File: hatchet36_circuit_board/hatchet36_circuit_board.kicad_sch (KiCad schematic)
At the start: 82 parts, among them J1 Conn_01x04_Female, SW1 SW_Push, SW10 SW_Push, SW11 SW_Push, SW12 SW_Push, SW13 SW_Push, SW14 SW_Push, SW15 SW_Push, SW16 SW_Push, SW17 SW_Push, SW18 SW_Push, SW19 SW_Push, SW2 SW_Push, SW20 SW_Push, SW21 SW_Push, SW22 SW_Push, SW23 SW_Push, SW24 SW_Push, SW25 SW_Push, SW26 SW_Push, SW27 SW_Push, SW28 SW_Push, SW29 SW_Push, SW3 SW_Push, SW30 SW_Push, SW31 SW_Push, SW32 SW_Push, SW33 SW_Push, SW34 SW_Push, SW35 SW_Push, SW36 SW_Push, SW37 SW_Push, SW38 SW_SPDT, SW4 SW_Push, SW5 SW_Push, SW6 SW_Push, SW7 SW_Push, SW8 SW_Push, SW9 SW_Push, U1 BL652

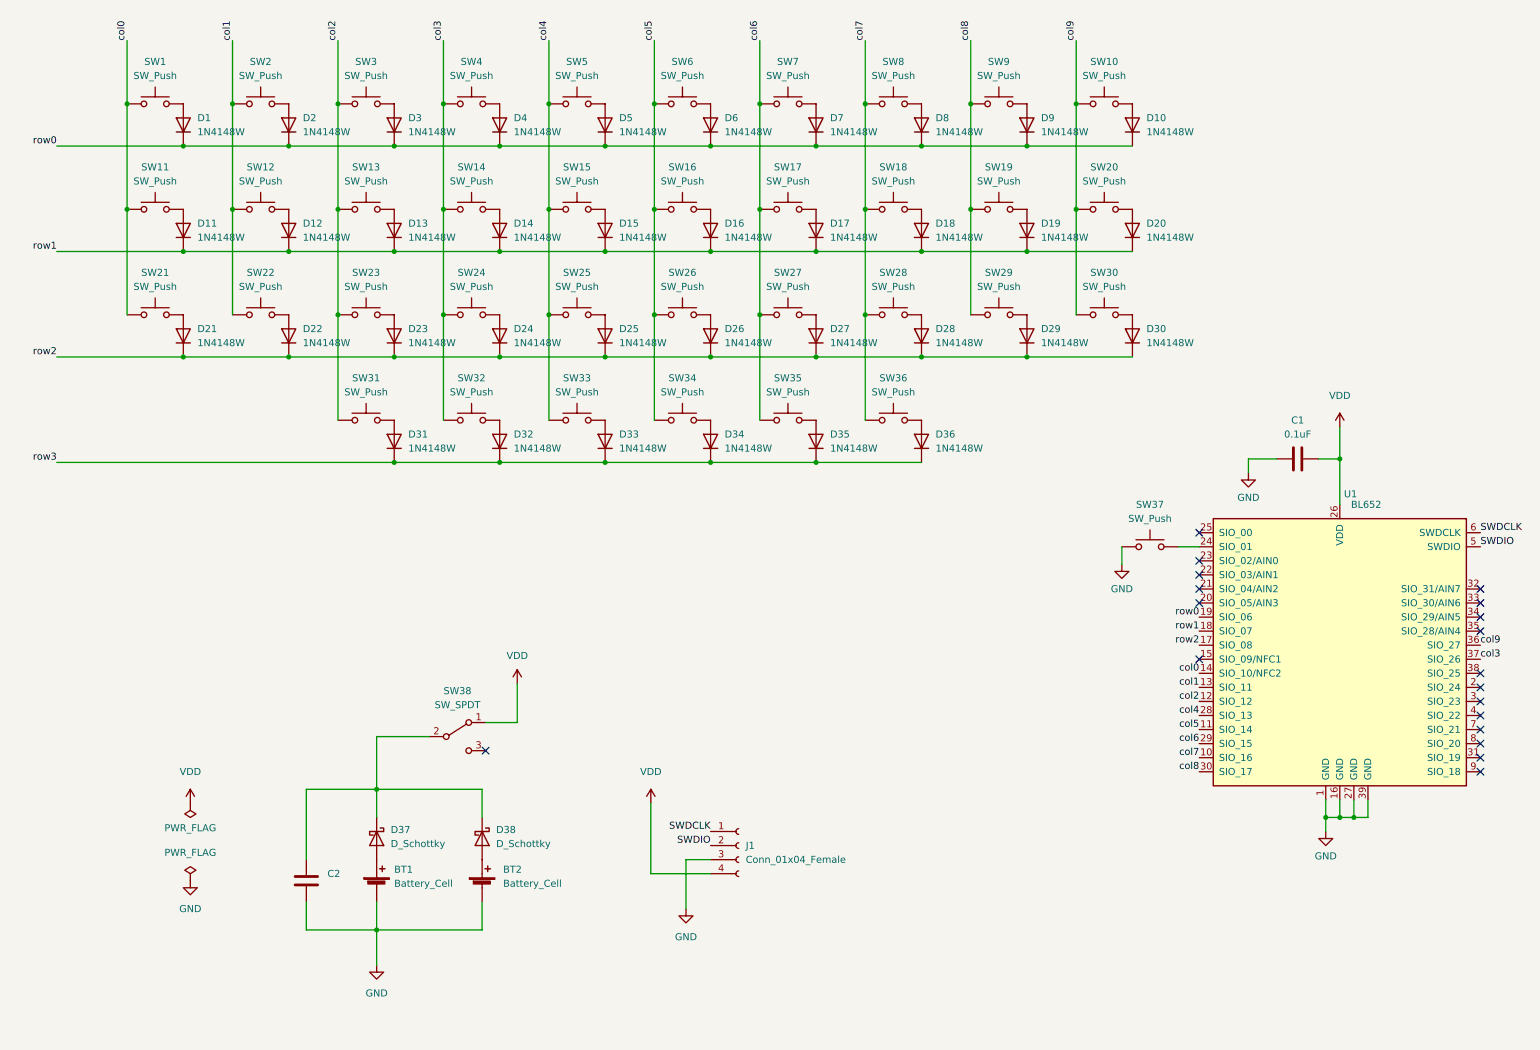
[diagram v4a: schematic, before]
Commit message: add connector
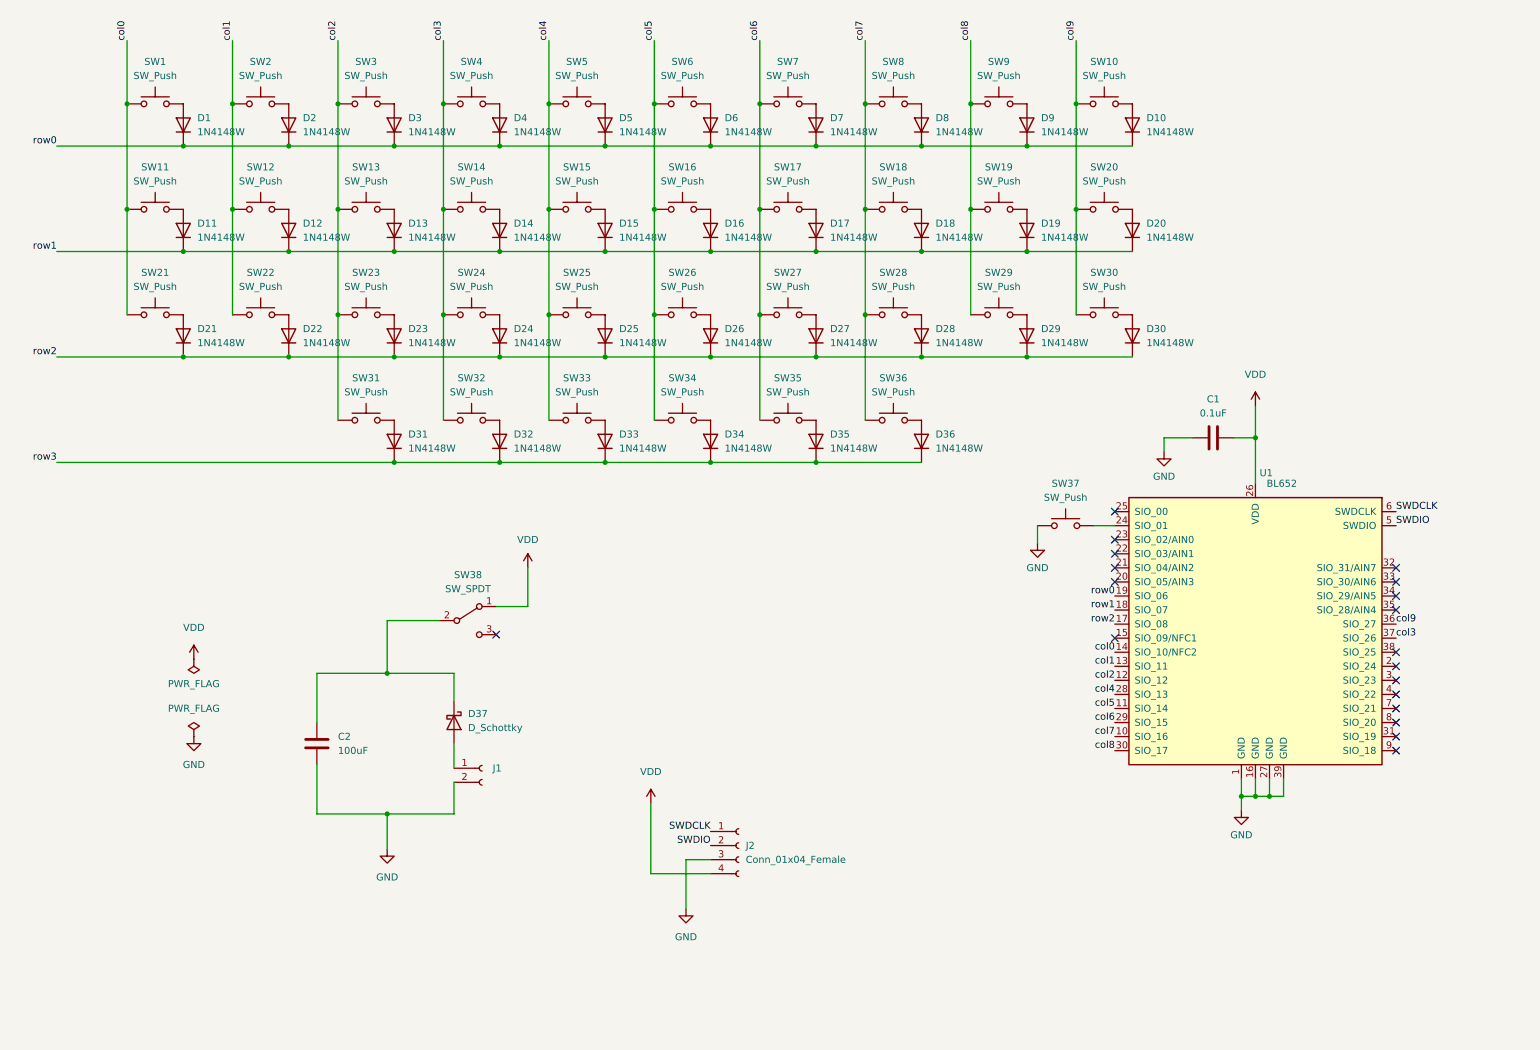
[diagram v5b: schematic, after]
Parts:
- removed BT1, BT2: Battery_Cell, symbol Device:Battery_Cell
- removed D37: D_Schottky, symbol Device:D_Schottky
- added J1: (no value), symbol Connector:Conn_01x02_Female
- C1: footprint (none) -> Capacitor_SMD:C_0805_2012Metric_Pad1.18x1.45mm_HandSolder
- C2: value (none) -> 100uF; footprint (none) -> Capacitor_SMD:C_1206_3216Metric_Pad1.33x1.80mm_HandSolder
- D37: renamed from D38; footprint (none) -> Diode_SMD:D_SOD-323
- J2: renamed from J1; footprint (none) -> locallib:programming_port
- SW1, SW10, SW11, SW12, SW13, SW14, SW15, SW16, SW17, SW18, SW19, SW2, SW20, SW21, SW22, SW23, SW24, SW25, SW26, SW27, SW28, SW29, SW3, SW30, SW31, SW32, SW33, SW34, SW35, SW36, SW4, SW5, SW6, SW7, SW8, SW9: footprint (none) -> locallib:Kailh-PG1350-1u-NoLED-mod
- SW37: footprint (none) -> locallib:SW_SPST_ALPS-SKRP
- SW38: footprint (none) -> locallib:slide_switch_vertical_01x03_pitch2mm
- U1: footprint (none) -> locallib:Laird_BL652_LongPad
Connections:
- net GND: now also J1.2 (Pin_2)
- net at D37.2 (A): now also J1.1 (Pin_1)
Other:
- moved on the sheet: C1, C2, D37, SW37, SW38, U1

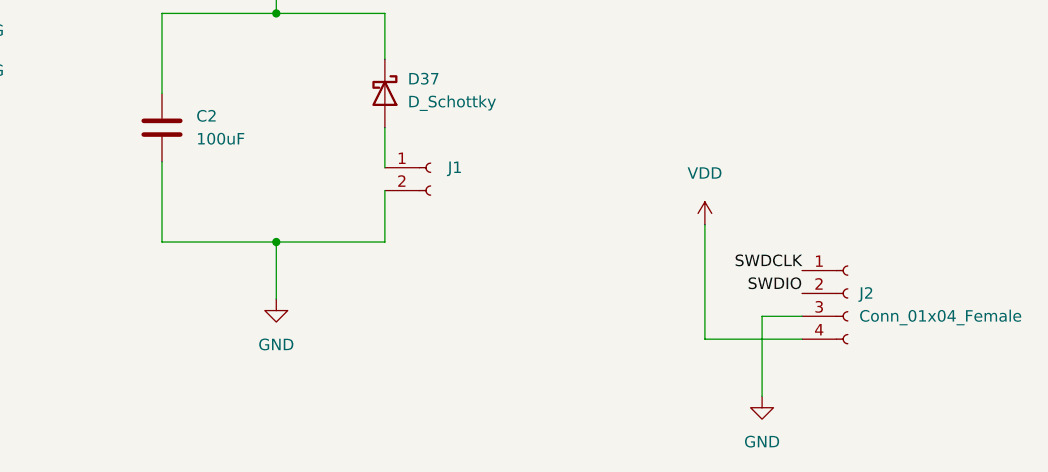
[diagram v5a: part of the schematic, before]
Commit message: mod for two battery
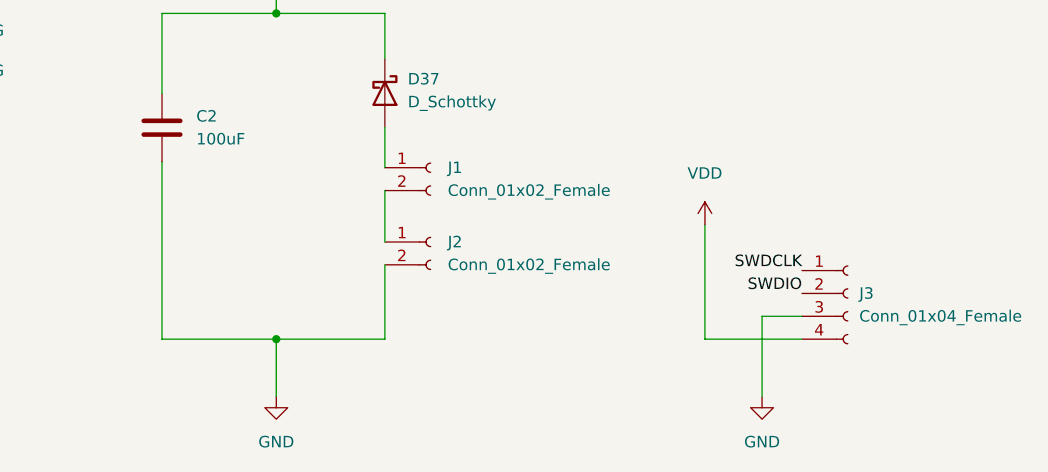
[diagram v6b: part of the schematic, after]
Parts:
- added J2: Conn_01x02_Female, symbol Connector:Conn_01x02_Female
- J1: value (none) -> Conn_01x02_Female
- renumbered J2 to J3
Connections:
- net GND: now also J2.2 (Pin_2); no longer J1.2 (Pin_2)
- new net: J1.2 (Pin_2), J2.1 (Pin_1)
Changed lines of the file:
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@@
   (junction (at 138.43 73.66) (diameter 0) (color 0 0 0 0)
   )
-  (junction (at 80.01 156.21) (diameter 0) (color 0 0 0 0)
+  (junction (at 80.01 167.005) (diameter 0) (color 0 0 0 0)
   )
   (junction (at 236.855 88.265) (diameter 0) (color 0 0 0 0)
@@
     (stroke (width 0) (type default) (color 0 0 0 0))
   )
-  (wire (pts (xy 67.31 147.32) (xy 67.31 156.21))
+  (wire (pts (xy 67.31 147.32) (xy 67.31 167.005))
     (stroke (width 0) (type default) (color 0 0 0 0))
   )
@@
     (stroke (width 0) (type default) (color 0 0 0 0))
   )
-  (wire (pts (xy 80.01 156.21) (xy 80.01 162.56))
-    (stroke (width 0) (type default) (color 0 0 0 0))
-  )
-  (wire (pts (xy 67.31 156.21) (xy 80.01 156.21))
+  (wire (pts (xy 80.01 167.005) (xy 80.01 173.355))
+    (stroke (width 0) (type default) (color 0 0 0 0))
+  )
+  (wire (pts (xy 67.31 167.005) (xy 80.01 167.005))
     (stroke (width 0) (type default) (color 0 0 0 0))
   )
@@
     (stroke (width 0) (type default) (color 0 0 0 0))
   )
-  (wire (pts (xy 92.075 156.21) (xy 80.01 156.21))
+  (wire (pts (xy 92.075 167.005) (xy 80.01 167.005))
     (stroke (width 0) (type default) (color 0 0 0 0))
   )
@@
   )
   (wire (pts (xy 20.32 73.66) (xy 43.18 73.66))
+    (stroke (width 0) (type default) (color 0 0 0 0))
+  )
+  (wire (pts (xy 92.075 158.75) (xy 92.075 167.005))
     (stroke (width 0) (type default) (color 0 0 0 0))
   )
@@
     (pin "2")
   )
-  (symbol (lib_id "power:GND") (at 80.01 162.56 0) (unit 1)
-    (in_bom yes) (on_board yes) (fields_autoplaced)
-    (property "Reference" "#PWR09" (id 0) (at 80.01 168.91 0)
-      (effects (font (size 1.27 1.27)) hide)
-    )
-    (property "Value" "GND" (id 1) (at 80.01 167.64 0))
-    (property "Footprint" "" (id 2) (at 80.01 162.56 0)
-      (effects (font (size 1.27 1.27)) hide)
-    )
-    (property "Datasheet" "" (id 3) (at 80.01 162.56 0)
+  (symbol (lib_id "power:GND") (at 80.01 173.355 0) (unit 1)
+    (in_bom yes) (on_board yes) (fields_autoplaced)
+    (property "Reference" "#PWR09" (id 0) (at 80.01 179.705 0)
+      (effects (font (size 1.27 1.27)) hide)
+    )
+    (property "Value" "GND" (id 1) (at 80.01 178.435 0))
+    (property "Footprint" "" (id 2) (at 80.01 173.355 0)
+      (effects (font (size 1.27 1.27)) hide)
+    )
+    (property "Datasheet" "" (id 3) (at 80.01 173.355 0)
       (effects (font (size 1.27 1.27)) hide)
     )
@@
       (effects (font (size 1.27 1.27)) (justify left))
     )
-    (property "Value" "" (id 1) (at 99.06 150.4949 0)
+    (property "Value" "Conn_01x02_Female" (id 1) (at 99.06 150.4949 0)
       (effects (font (size 1.27 1.27)) (justify left))
     )
@@
     (pin "2")
   )
+  (symbol (lib_id "Connector:Conn_01x02_Female") (at 97.155 156.21 0) (unit 1)
+    (in_bom yes) (on_board yes) (fields_autoplaced)
+    (property "Reference" "J2" (id 0) (at 99.06 156.2099 0)
+      (effects (font (size 1.27 1.27)) (justify left))
+    )
+    (property "Value" "Conn_01x02_Female" (id 1) (at 99.06 158.7499 0)
+      (effects (font (size 1.27 1.27)) (justify left))
+    )
+    (property "Footprint" "" (id 2) (at 97.155 156.21 0)
+      (effects (font (size 1.27 1.27)) hide)
+    )
+    (property "Datasheet" "~" (id 3) (at 97.155 156.21 0)
+      (effects (font (size 1.27 1.27)) hide)
+    )
+    (pin "1")
+    (pin "2")
+  )
   (symbol (lib_id "Switch:SW_Push") (at 171.45 27.94 0) (unit 1)
     (in_bom yes) (on_board yes) (fields_autoplaced)
@@
   (symbol (lib_id "Connector:Conn_01x04_Female") (at 143.51 161.925 0) (unit 1)
     (in_bom yes) (on_board yes) (fields_autoplaced)
-    (property "Reference" "J2" (id 0) (at 144.78 161.9249 0)
+    (property "Reference" "J3" (id 0) (at 144.78 161.9249 0)
       (effects (font (size 1.27 1.27)) (justify left))
     )
@@
     )
     (path "/88af43ad-0ce6-423b-bab0-2a1dbd5eaa54"
-      (reference "J1") (unit 1) (value "Conn_01x02_Female") (footprint "Connector_JST:JST_PH_S2B-PH-K_1x02_P2.00mm_Horizontal")
+      (reference "J1") (unit 1) (value "Conn_01x02_Female") (footprint "TestPoint:TestPoint_2Pads_Pitch2.54mm_Drill0.8mm")
+    )
+    (path "/ad996359-1b62-4295-9488-a9308d8aa53b"
+      (reference "J2") (unit 1) (value "Conn_01x02_Female") (footprint "TestPoint:TestPoint_2Pads_Pitch2.54mm_Drill0.8mm")
     )
     (path "/f4b00c54-9ad1-49cc-a893-af751b7bbde3"
-      (reference "J2") (unit 1) (value "Conn_01x04_Female") (footprint "locallib:programming_port")
+      (reference "J3") (unit 1) (value "Conn_01x04_Female") (footprint "locallib:programming_port")
     )
     (path "/a357589c-4160-43cf-bb11-976072c8dee0"

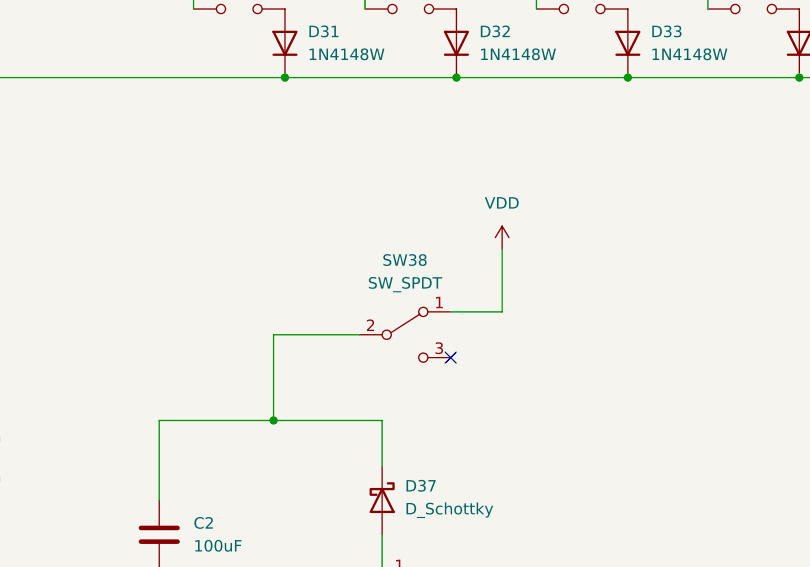
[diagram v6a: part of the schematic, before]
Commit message: put all parts on pcb
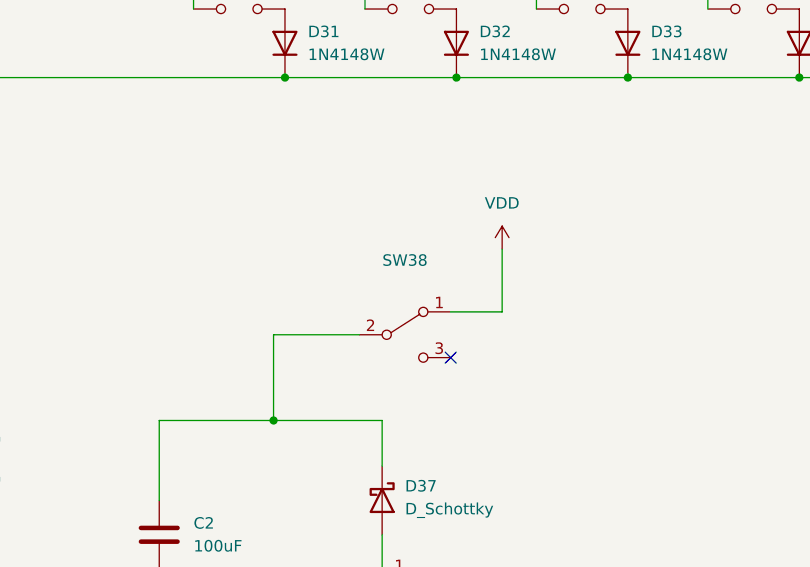
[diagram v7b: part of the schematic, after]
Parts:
- SW38: value SW_SPDT -> (none); footprint locallib:slide_switch_vertical_01x03_pitch2mm -> (none)
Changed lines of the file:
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@@
     (in_bom yes) (on_board yes) (fields_autoplaced)
     (property "Reference" "SW38" (id 0) (at 94.615 113.03 0))
-    (property "Value" "SW_SPDT" (id 1) (at 94.615 115.57 0))
-    (property "Footprint" "locallib:slide_switch_vertical_01x03_pitch2mm" (id 2) (at 94.615 121.285 0)
+    (property "Value" "" (id 1) (at 94.615 115.57 0))
+    (property "Footprint" "" (id 2) (at 94.615 121.285 0)
       (effects (font (size 1.27 1.27)) hide)
     )
@@
     )
     (path "/88af43ad-0ce6-423b-bab0-2a1dbd5eaa54"
-      (reference "J1") (unit 1) (value "Conn_01x02_Female") (footprint "TestPoint:TestPoint_2Pads_Pitch2.54mm_Drill0.8mm")
+      (reference "J1") (unit 1) (value "Conn_01x02_Female") (footprint "Connector_PinHeader_2.00mm:PinHeader_1x02_P2.00mm_Vertical")
     )
     (path "/ad996359-1b62-4295-9488-a9308d8aa53b"
-      (reference "J2") (unit 1) (value "Conn_01x02_Female") (footprint "TestPoint:TestPoint_2Pads_Pitch2.54mm_Drill0.8mm")
+      (reference "J2") (unit 1) (value "Conn_01x02_Female") (footprint "Connector_PinHeader_2.00mm:PinHeader_1x02_P2.00mm_Vertical")
     )
     (path "/f4b00c54-9ad1-49cc-a893-af751b7bbde3"
@@
     )
     (path "/cb61f6a9-cf62-4a04-aa61-3fe07a0b0bd3"
-      (reference "SW38") (unit 1) (value "SW_SPDT") (footprint "locallib:slide_switch_vertical_01x03_pitch2mm")
+      (reference "SW38") (unit 1) (value "SW_SPDT") (footprint "locallib:SW_Slide_1P2T_CK_OS102011MS2Q_SmallPad")
     )
     (path "/73846744-8199-4c16-b04a-3244ef0b5a6a"
